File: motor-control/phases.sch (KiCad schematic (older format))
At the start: 42 parts, among them Q1 csd19505kcs, Q10 csd19505kcs, Q11 csd19505kcs, Q12 csd19505kcs, Q2 csd19505kcs, Q3 csd19505kcs, Q4 csd19505kcs, Q5 csd19505kcs, Q6 csd19505kcs, Q7 csd19505kcs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

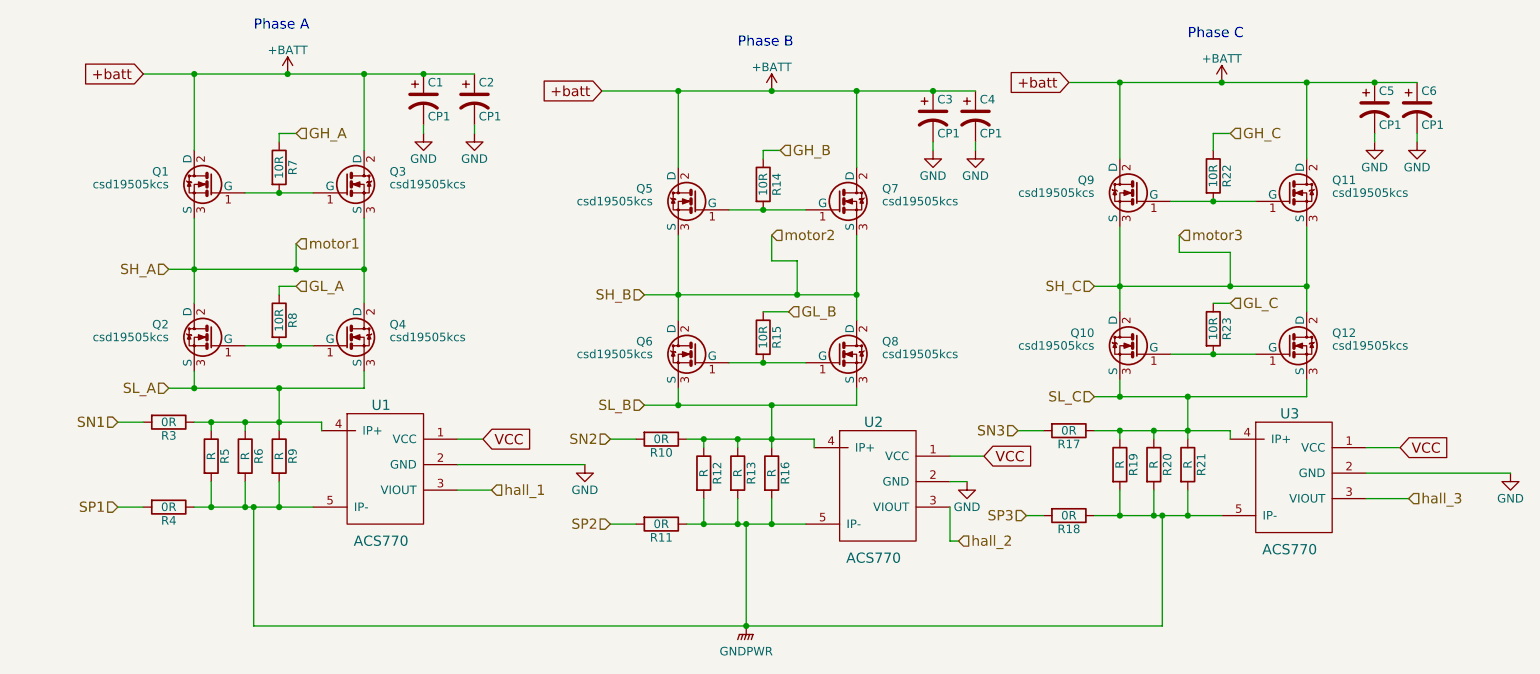
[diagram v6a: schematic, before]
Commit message: Modified Schematic Comp resist/cap vals, added bom
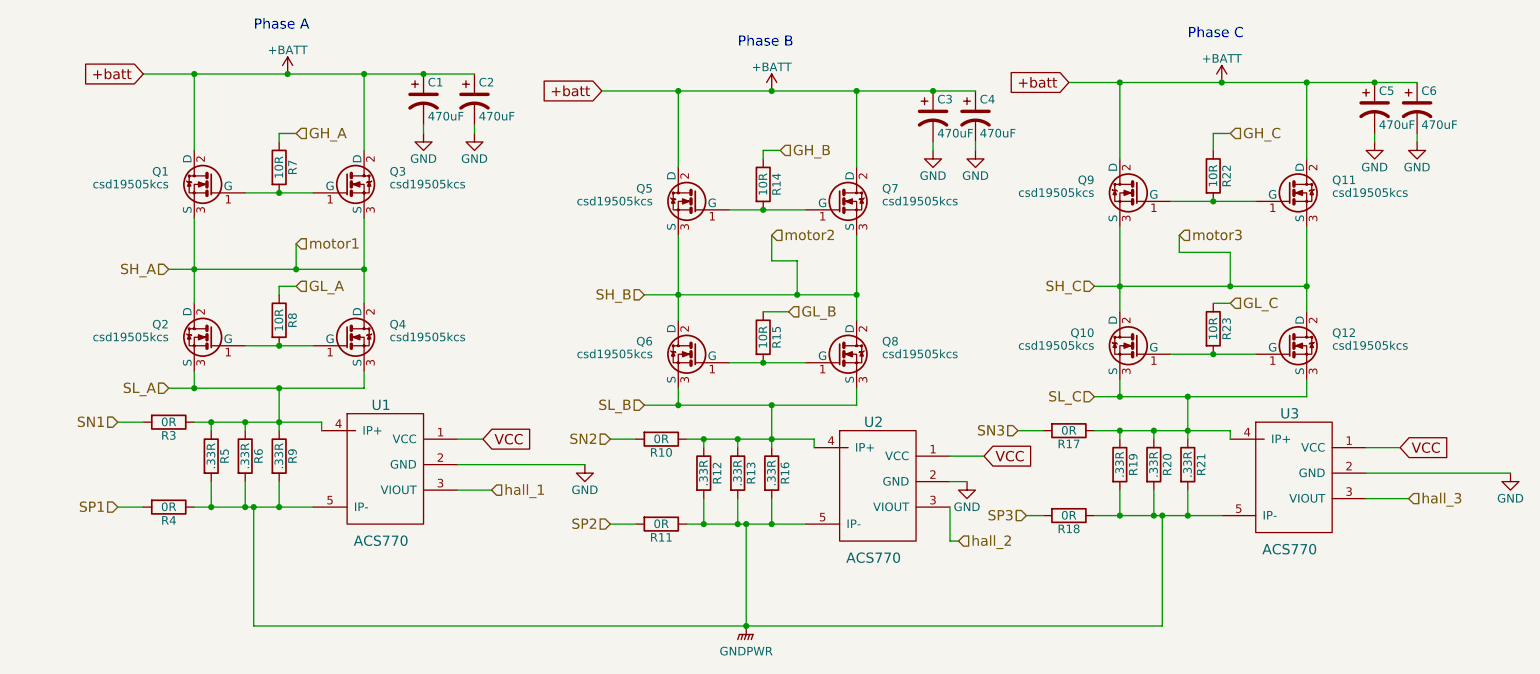
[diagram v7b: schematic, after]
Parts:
- C1, C2, C3, C4, C5, C6: value CP1 -> 470uF
- R12, R13, R16, R19, R20, R21, R5, R6, R9: value R -> .33R
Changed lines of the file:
@@
 P 4650 2100
 F 0 "C1" H 4675 2200 50  0000 L CNN
-F 1 "CP1" H 4675 2000 50  0000 L CNN
+F 1 "470uF" H 4675 2000 50  0000 L CNN
 F 2 "Capacitors_ThroughHole:C_Radial_D16_L30_P7.5" H 4650 2100 60  0001 C CNN
 F 3 "" H 4650 2100 60  0000 C CNN
@@
 P 3800 4200
 F 0 "R9" V 3880 4200 50  0000 C CNN
-F 1 "R" V 3800 4200 50  0000 C CNN
+F 1 ".33R" V 3800 4200 50  0000 C CNN
 F 2 "Resistors_ThroughHole:Resistor_Vertical_RM7.5mm" V 3730 4200 30  0001 C CNN
 F 3 "" H 3800 4200 30  0000 C CNN
@@
 P 3600 4200
 F 0 "R6" V 3680 4200 50  0000 C CNN
-F 1 "R" V 3600 4200 50  0000 C CNN
+F 1 ".33R" V 3600 4200 50  0000 C CNN
 F 2 "Resistors_ThroughHole:Resistor_Vertical_RM7.5mm" V 3530 4200 30  0001 C CNN
 F 3 "" H 3600 4200 30  0000 C CNN
@@
 P 3400 4200
 F 0 "R5" V 3480 4200 50  0000 C CNN
-F 1 "R" V 3400 4200 50  0000 C CNN
+F 1 ".33R" V 3400 4200 50  0000 C CNN
 F 2 "Resistors_ThroughHole:Resistor_Vertical_RM7.5mm" V 3330 4200 30  0001 C CNN
 F 3 "" H 3400 4200 30  0000 C CNN
@@
 P 7650 2200
 F 0 "C3" H 7675 2300 50  0000 L CNN
-F 1 "CP1" H 7675 2100 50  0000 L CNN
+F 1 "470uF" H 7675 2100 50  0000 L CNN
 F 2 "Capacitors_ThroughHole:C_Radial_D16_L30_P7.5" H 7650 2200 60  0001 C CNN
 F 3 "" H 7650 2200 60  0000 C CNN
@@
 P 6300 4300
 F 0 "R12" V 6380 4300 50  0000 C CNN
-F 1 "R" V 6300 4300 50  0000 C CNN
+F 1 ".33R" V 6300 4300 50  0000 C CNN
 F 2 "Resistors_ThroughHole:Resistor_Vertical_RM7.5mm" V 6230 4300 30  0001 C CNN
 F 3 "" H 6300 4300 30  0000 C CNN
@@
 P 6500 4300
 F 0 "R13" V 6580 4300 50  0000 C CNN
-F 1 "R" V 6500 4300 50  0000 C CNN
+F 1 ".33R" V 6500 4300 50  0000 C CNN
 F 2 "Resistors_ThroughHole:Resistor_Vertical_RM7.5mm" V 6430 4300 30  0001 C CNN
 F 3 "" H 6500 4300 30  0000 C CNN
@@
 P 6700 4300
 F 0 "R16" V 6780 4300 50  0000 C CNN
-F 1 "R" V 6700 4300 50  0000 C CNN
+F 1 ".33R" V 6700 4300 50  0000 C CNN
 F 2 "Resistors_ThroughHole:Resistor_Vertical_RM7.5mm" V 6630 4300 30  0001 C CNN
 F 3 "" H 6700 4300 30  0000 C CNN
@@
 P 10250 2150
 F 0 "C5" H 10275 2250 50  0000 L CNN
-F 1 "CP1" H 10275 2050 50  0000 L CNN
+F 1 "470uF" H 10275 2050 50  0000 L CNN
 F 2 "Capacitors_ThroughHole:C_Radial_D16_L30_P7.5" H 10250 2150 60  0001 C CNN
 F 3 "" H 10250 2150 60  0000 C CNN
@@
 P 8750 4250
 F 0 "R19" V 8830 4250 50  0000 C CNN
-F 1 "R" V 8750 4250 50  0000 C CNN
+F 1 ".33R" V 8750 4250 50  0000 C CNN
 F 2 "Resistors_ThroughHole:Resistor_Vertical_RM7.5mm" V 8680 4250 30  0001 C CNN
 F 3 "" H 8750 4250 30  0000 C CNN
@@
 P 8950 4250
 F 0 "R20" V 9030 4250 50  0000 C CNN
-F 1 "R" V 8950 4250 50  0000 C CNN
+F 1 ".33R" V 8950 4250 50  0000 C CNN
 F 2 "Resistors_ThroughHole:Resistor_Vertical_RM7.5mm" V 8880 4250 30  0001 C CNN
 F 3 "" H 8950 4250 30  0000 C CNN
@@
 P 9150 4250
 F 0 "R21" V 9230 4250 50  0000 C CNN
-F 1 "R" V 9150 4250 50  0000 C CNN
+F 1 ".33R" V 9150 4250 50  0000 C CNN
 F 2 "Resistors_ThroughHole:Resistor_Vertical_RM7.5mm" V 9080 4250 30  0001 C CNN
 F 3 "" H 9150 4250 30  0000 C CNN
@@
 P 4950 2100
 F 0 "C2" H 4975 2200 50  0000 L CNN
-F 1 "CP1" H 4975 2000 50  0000 L CNN
+F 1 "470uF" H 4975 2000 50  0000 L CNN
 F 2 "Capacitors_ThroughHole:C_Radial_D16_L30_P7.5" H 4950 2100 60  0001 C CNN
 F 3 "" H 4950 2100 60  0000 C CNN
@@
 P 7900 2200
 F 0 "C4" H 7925 2300 50  0000 L CNN
-F 1 "CP1" H 7925 2100 50  0000 L CNN
+F 1 "470uF" H 7925 2100 50  0000 L CNN
 F 2 "Capacitors_ThroughHole:C_Radial_D16_L30_P7.5" H 7900 2200 60  0001 C CNN
 F 3 "" H 7900 2200 60  0000 C CNN
@@
 P 10500 2150
 F 0 "C6" H 10525 2250 50  0000 L CNN
-F 1 "CP1" H 10525 2050 50  0000 L CNN
+F 1 "470uF" H 10525 2050 50  0000 L CNN
 F 2 "Capacitors_ThroughHole:C_Radial_D16_L30_P7.5" H 10500 2150 60  0001 C CNN
 F 3 "" H 10500 2150 60  0000 C CNN
